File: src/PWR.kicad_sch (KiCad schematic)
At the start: 32 parts, among them J1 USB_C_Receptacle_USB2.0_16P, J5 Conn_01x02, J6 WJ15EDGK-3.81-2P, Q1 AO3401A, Q2 AO3401A, Q3 BC817-40-7-F, Q4 BC817-40-7-F, Q5 BC817-40-7-F, U11 TPS70950DBVR, U4 TPS54302DDCR

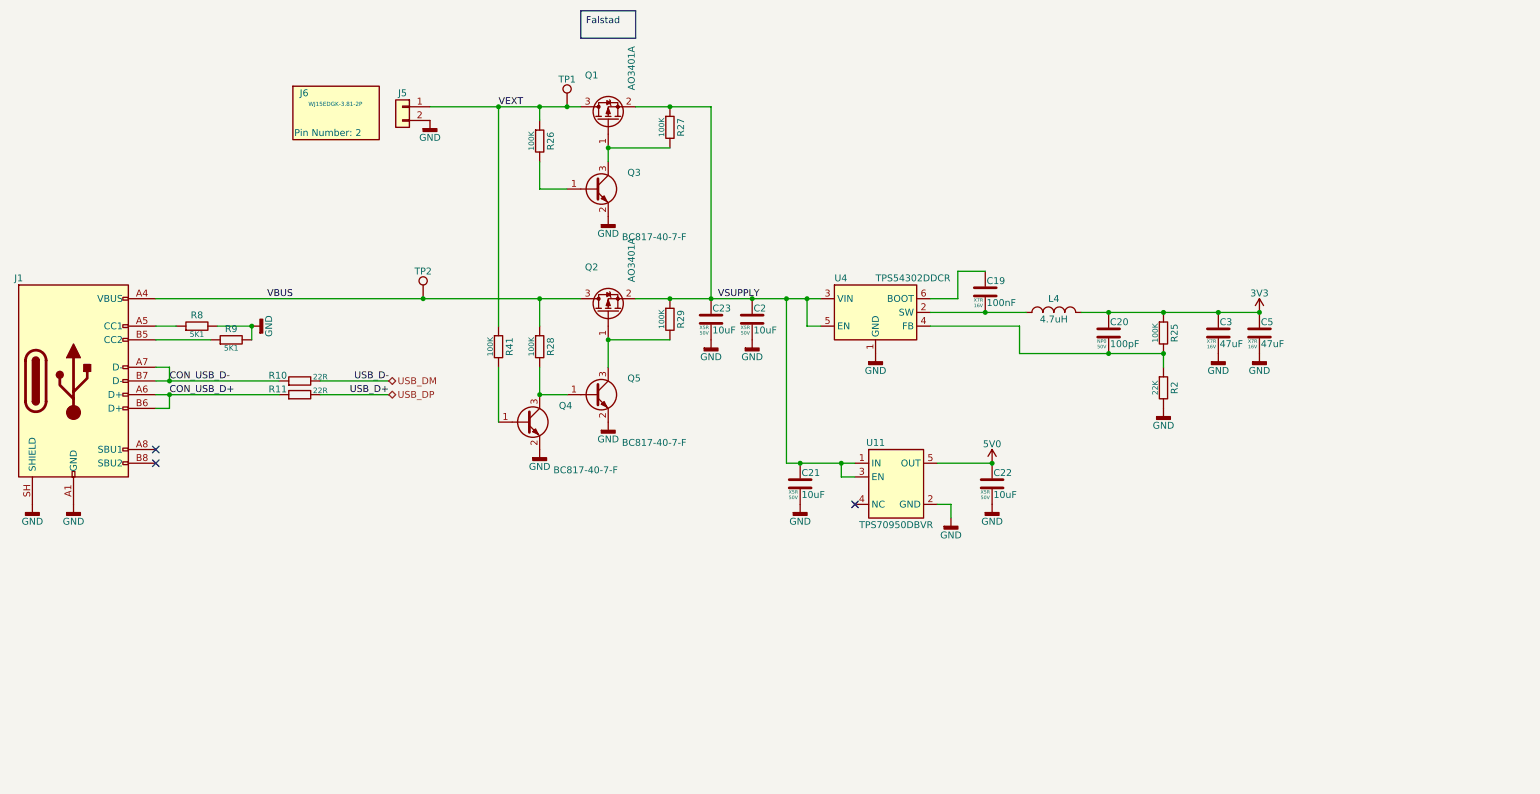
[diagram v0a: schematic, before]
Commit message: V3.1 first changes
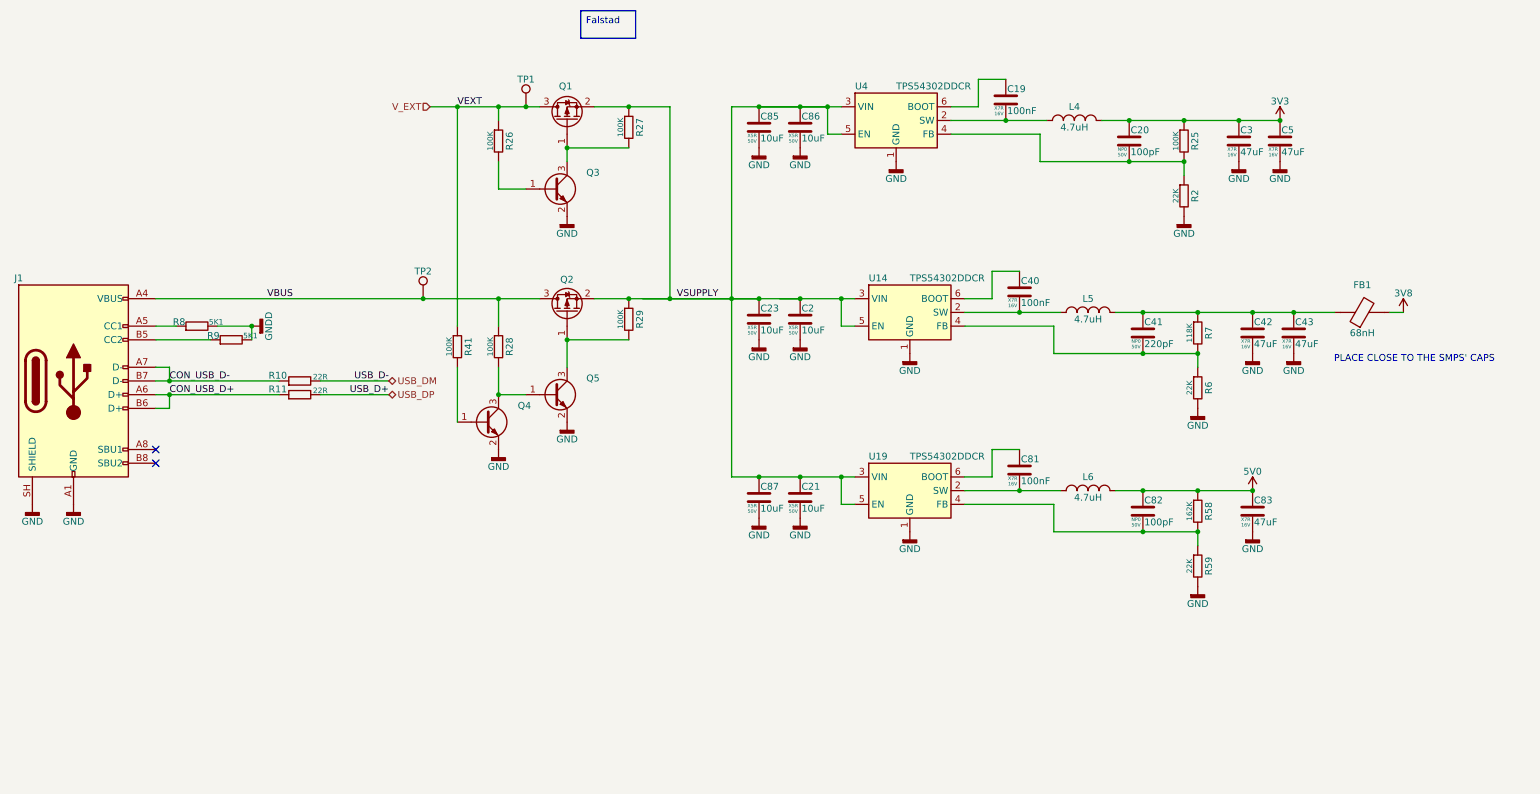
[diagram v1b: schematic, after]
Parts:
- removed C22: 10uF, 7Sigma:C_0805_2012Metric, symbol Capacitor:GRM21BR61H106KE43L
- removed J5: Conn_01x02, 7Sigma:PhoenixContact_MC_1,5_2-G-3.81_1x02_P3.81mm_Horizontal, symbol Connectors:WJ15EDGRC-3.81-2P
- removed J6: WJ15EDGK-3.81-2P, 7Sigma:TerminalBlock_Plug_Invisible, symbol Connectors:WJ15EDGK-3.81-2P
- removed U11: TPS70950DBVR, 7Sigma:SOT-23-5, symbol ICs:TPS70950DBVR
- added C40, C81: 100nF, 7Sigma:C_0402_1005Metric, symbol Capacitor:CL05B104KO5NNNC
- added C41: 220pF, 7Sigma:C_0402_1005Metric, symbol Capacitor:CC0402JRNPO9BN221
- added C42, C43, C83: 47uF, 7Sigma:C_1210_3225Metric, symbol Capacitor:CS3225X7R476K160NRL
- added C82: 100pF, 7Sigma:C_0402_1005Metric, symbol Capacitor:CC0402JRNPO9BN101
- added C85, C86, C87: 10uF, 7Sigma:C_0805_2012Metric, symbol Capacitor:GRM21BR61H106KE43L
- added FB1: 68nH, 7Sigma:L_0603_1608Metric, symbol Inductors:BLM18EG101TN1D
- added L5, L6: 4.7uH, 7Sigma:L_Changjiang_FTC404030S, symbol Inductors:FTC404030S4R7MGCA
- added R58: 162K, 7Sigma:R_0402_1005Metric, symbol Resistor:0402WGF1623TCE
- added R59, R6: 22K, 7Sigma:R_0402_1005Metric, symbol Resistor:0402WGF2202TCE
- added R7: 118K, 7Sigma:R_0402_1005Metric, symbol Resistor:0402WGF1183TCE
- added U14, U19: TPS54302DDCR, 7Sigma:SOT-23-6, symbol ICs:TPS54302DDCR
- Q1, Q2, Q3, Q4, Q5: footprint 7Sigma:SOT-23 -> 7Sigma:SOT-23-3
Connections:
- net 5V0: now also C82.1, C83.1, L6.2, R58.1
- net GND: now also C42.2, C43.2, C83.2, C85.2, C86.2, C87.2, R59.2, R6.2, U14.1 (GND), U19.1 (GND); no longer R8.2, R9.2
- net VSUPPLY: now also C85.1, C86.1, C87.1, U14.3 (VIN), U14.5 (EN), U19.3 (VIN), U19.5 (EN)
- net VEXT renamed V_EXT
- new net: C41.1, C42.1, C43.1, FB1.1, L5.2, R7.1
- new net: C81.1, U19.6 (BOOT)
- new net: C81.2, L6.1, U19.2 (SW)
- new net: C41.2, R6.1, R7.2, U14.4 (FB)
- new net: C82.2, R58.2, R59.1, U19.4 (FB)
- new net: C40.1, U14.6 (BOOT)
- new net: C40.2, L5.1, U14.2 (SW)
- new net 3V8: FB1.2
- new net GNDD: R8.2, R9.2
- no-connect marks 3 -> 2
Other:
- note added: "PLACE CLOSE TO THE SMPS' CAPS"
- moved on the sheet: C19, C2, C20, C23, C3, C5, L4, Q1, Q2, Q3, Q4, Q5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

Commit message: ongoing work
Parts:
- removed Q3, Q4, Q5: BC817-40-7-F, 7Sigma:SOT-23-3, symbol Transistors:BC817-40-7-F
- removed R29, R41: 100K, 7Sigma:R_0402_1005Metric, symbol Resistor:0402WGF1003TCE
- added C90, C91, C92: 100nF, 7Sigma:C_0402_1005Metric, symbol Capacitor:CL05B104KO5NNNC
- added C93: 47uF, 7Sigma:C_1210_3225Metric, symbol Capacitor:CS3225X7R476K160NRL
- added D11: SS34, 7Sigma:D_SMA, symbol Diodes:SS34
- added D12: 5V1, 7Sigma:D_SOD-123, symbol Diodes:BZT52C5V1
- added Q11, Q12, Q13: SI2308A, 7Sigma:SOT-23-3, symbol Transistors:SI2308A
- added R30: 5K1, 7Sigma:R_0402_1005Metric, symbol Resistor:0402WGF5101TCE
- added R37: 374K, 7Sigma:R_0402_1005Metric, symbol Resistor:0402WGF3743TCE
- added R39: 100K, 7Sigma:R_0402_1005Metric, symbol Resistor:0402WGF1003TCE
- added R48, R55, R56, R71, R72: 22K, 7Sigma:R_0402_1005Metric, symbol Resistor:0402WGF2202TCE
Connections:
- net GNDD is gone; now on net GND: R8.2, R9.2
- net 5V0: now also C93.1, D11.1 (K)
- net GND: now also R28.2, C90.2, C91.2, C92.2, C93.2, D12.2 (A), Q11.2 (S), Q12.2 (S), Q13.2 (S), R30.1, R39.2, R55.2
- net VBUS: now also D11.2 (A), R71.1; no longer R28.1
- net VSUPPLY: now also C90.1, C91.1, C92.1, R37.1, R48.1, R56.1; no longer R27.1, U14.5 (EN), U19.5 (EN), U4.5 (EN)
- net V_EXT: now also R72.1
- net at Q1.1 (G): now also R27.1, R48.2; no longer R27.2
- net nSOURCE_USB: now reaches Q2.1 (G)
- net nSOURCE_USB: now also Q12.3 (D), R56.2
- net at R26.2: now also Q13.1 (G), R55.1
- new net: Q13.3 (D), R27.2
- new net: Q11.1 (G), R30.2, R72.2
- new net: Q11.3 (D), Q12.1 (G), R28.1, R71.2
- new net: D12.1 (K), R37.2, R39.1, U19.5 (EN)
- no-connect marks 2 -> 4
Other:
- note added: "DISABLE WHEN EXT. voltage applied (higher than USB)"
- moved on the sheet: C19, C2, C20, C21, C23, C3, C40, C41, C42, C43, C5, C85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

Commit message: Layout progress
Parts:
- C19, C40, C81, C90, C91, C92: Price @1 USD (none) -> 0.0015; Price @100 USD (none) -> 0.0015; Price @Bulk USD (none) -> 0.0012; Price Bulk Qty (none) -> 1000; Price Source (none) -> LCSC; Price Updated (none) -> 2026-05-14
- C2, C21, C23, C85, C86, C87: Price @1 USD (none) -> 0.0690; Price @100 USD (none) -> 0.0561; Price @Bulk USD (none) -> 0.0494; Price Bulk Qty (none) -> 300; Price Source (none) -> LCSC; Price Updated (none) -> 2026-05-14
- C20, C82: Price @1 USD (none) -> 0.0012; Price @100 USD (none) -> 0.0012; Price @Bulk USD (none) -> 0.0010; Price Bulk Qty (none) -> 1000; Price Source (none) -> LCSC; Price Updated (none) -> 2026-05-14
- C3, C42, C43, C5, C83, C93: Price @1 USD (none) -> 0.1071; Price @100 USD (none) -> 0.0850; Price @Bulk USD (none) -> 0.0636; Price Bulk Qty (none) -> 1000; Price Source (none) -> LCSC; Price Updated (none) -> 2026-05-14
- C41: Price @1 USD (none) -> 0.0029; Price @100 USD (none) -> 0.0029; Price @Bulk USD (none) -> 0.0022; Price Bulk Qty (none) -> 1000; Price Source (none) -> LCSC; Price Updated (none) -> 2026-05-14
- D11: Price @1 USD (none) -> 0.0278; Price @100 USD (none) -> 0.0278; Price @Bulk USD (none) -> 0.0193; Price Bulk Qty (none) -> 600; Price Source (none) -> LCSC; Price Updated (none) -> 2026-05-14
- D12: Price @1 USD (none) -> 0.0131; Price @100 USD (none) -> 0.0131; Price @Bulk USD (none) -> 0.0121; Price Bulk Qty (none) -> 500; Price Source (none) -> LCSC; Price Updated (none) -> 2026-05-14
- FB1: Price @1 USD (none) -> 0.0538; Price @100 USD (none) -> 0.0538; Price @Bulk USD (none) -> 0.0408; Price Bulk Qty (none) -> 600; Price Source (none) -> LCSC; Price Updated (none) -> 2026-05-14
- J1: Price @1 USD (none) -> 0.3864; Price @100 USD (none) -> 0.3059; Price @Bulk USD (none) -> 0.2316; Price Bulk Qty (none) -> 1000; Price Source (none) -> LCSC; Price Updated (none) -> 2026-05-14
- L4, L5, L6: Price @1 USD (none) -> 0.2442; Price @100 USD (none) -> 0.1909; Price @Bulk USD (none) -> 0.1397; Price Bulk Qty (none) -> 500; Price Source (none) -> LCSC; Price Updated (none) -> 2026-05-14
- Q1, Q2: Price @1 USD (none) -> 0.0589; Price @100 USD (none) -> 0.0474; Price @Bulk USD (none) -> 0.0415; Price Bulk Qty (none) -> 300; Price Source (none) -> LCSC; Price Updated (none) -> 2026-05-14
- Q11, Q12, Q13: Price @1 USD (none) -> 0.0364; Price @100 USD (none) -> 0.0284; Price @Bulk USD (none) -> 0.0242; Price Bulk Qty (none) -> 300; Price Source (none) -> LCSC; Price Updated (none) -> 2026-05-14
- R10, R11, R58: Price @1 USD (none) -> 0.0007; Price @100 USD (none) -> 0.0007; Price @Bulk USD (none) -> 0.0006; Price Bulk Qty (none) -> 1000; Price Source (none) -> LCSC; Price Updated (none) -> 2026-05-14
- R2, R48, R55, R56, R59, R6, R71: Price @1 USD (none) -> 0.0010; Price @100 USD (none) -> 0.0010; Price @Bulk USD (none) -> 0.0008; Price Bulk Qty (none) -> 1000; Price Source (none) -> LCSC; Price Updated (none) -> 2026-05-14
- R25, R26, R27, R28, R39, R8, R9: Price @1 USD (none) -> 0.0009; Price @100 USD (none) -> 0.0009; Price @Bulk USD (none) -> 0.0007; Price Bulk Qty (none) -> 1000; Price Source (none) -> LCSC; Price Updated (none) -> 2026-05-14
- R30: value 5K1 -> 22K; symbol Resistor:0402WGF5101TCE -> Resistor:0402WGF2202TCE; LCSC Part C25905 -> C25768; Manufacturer Part Number 1 0402WGF5101TCE -> 0402WGF2202TCE; Price @1 USD (none) -> 0.0010; Price @100 USD (none) -> 0.0010; Price @Bulk USD (none) -> 0.0008; Price Bulk Qty (none) -> 1000; Price Source (none) -> LCSC; Price Updated (none) -> 2026-05-14; Supplier Part Number 1 C25905 -> C25768
- R37, R7: Price @1 USD (none) -> 0.0004; Price @100 USD (none) -> 0.0004; Price @Bulk USD (none) -> 0.0004; Price Bulk Qty (none) -> 100; Price Source (none) -> LCSC; Price Updated (none) -> 2026-05-14
- R72: value 22K -> 100K; symbol Resistor:0402WGF2202TCE -> Resistor:0402WGF1003TCE; LCSC Part C25768 -> C25741; Manufacturer Part Number 1 0402WGF2202TCE -> 0402WGF1003TCE; Price @1 USD (none) -> 0.0009; Price @100 USD (none) -> 0.0009; Price @Bulk USD (none) -> 0.0007; Price Bulk Qty (none) -> 1000; Price Source (none) -> LCSC; Price Updated (none) -> 2026-05-14; Supplier Part Number 1 C25768 -> C25741
- U14, U19, U4: Price @1 USD (none) -> 0.2927; Price @100 USD (none) -> 0.2293; Price @Bulk USD (none) -> 0.1707; Price Bulk Qty (none) -> 500; Price Source (none) -> LCSC; Price Updated (none) -> 2026-05-14
